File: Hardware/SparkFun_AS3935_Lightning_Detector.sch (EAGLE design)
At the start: 30 parts, among them U1 AS3935

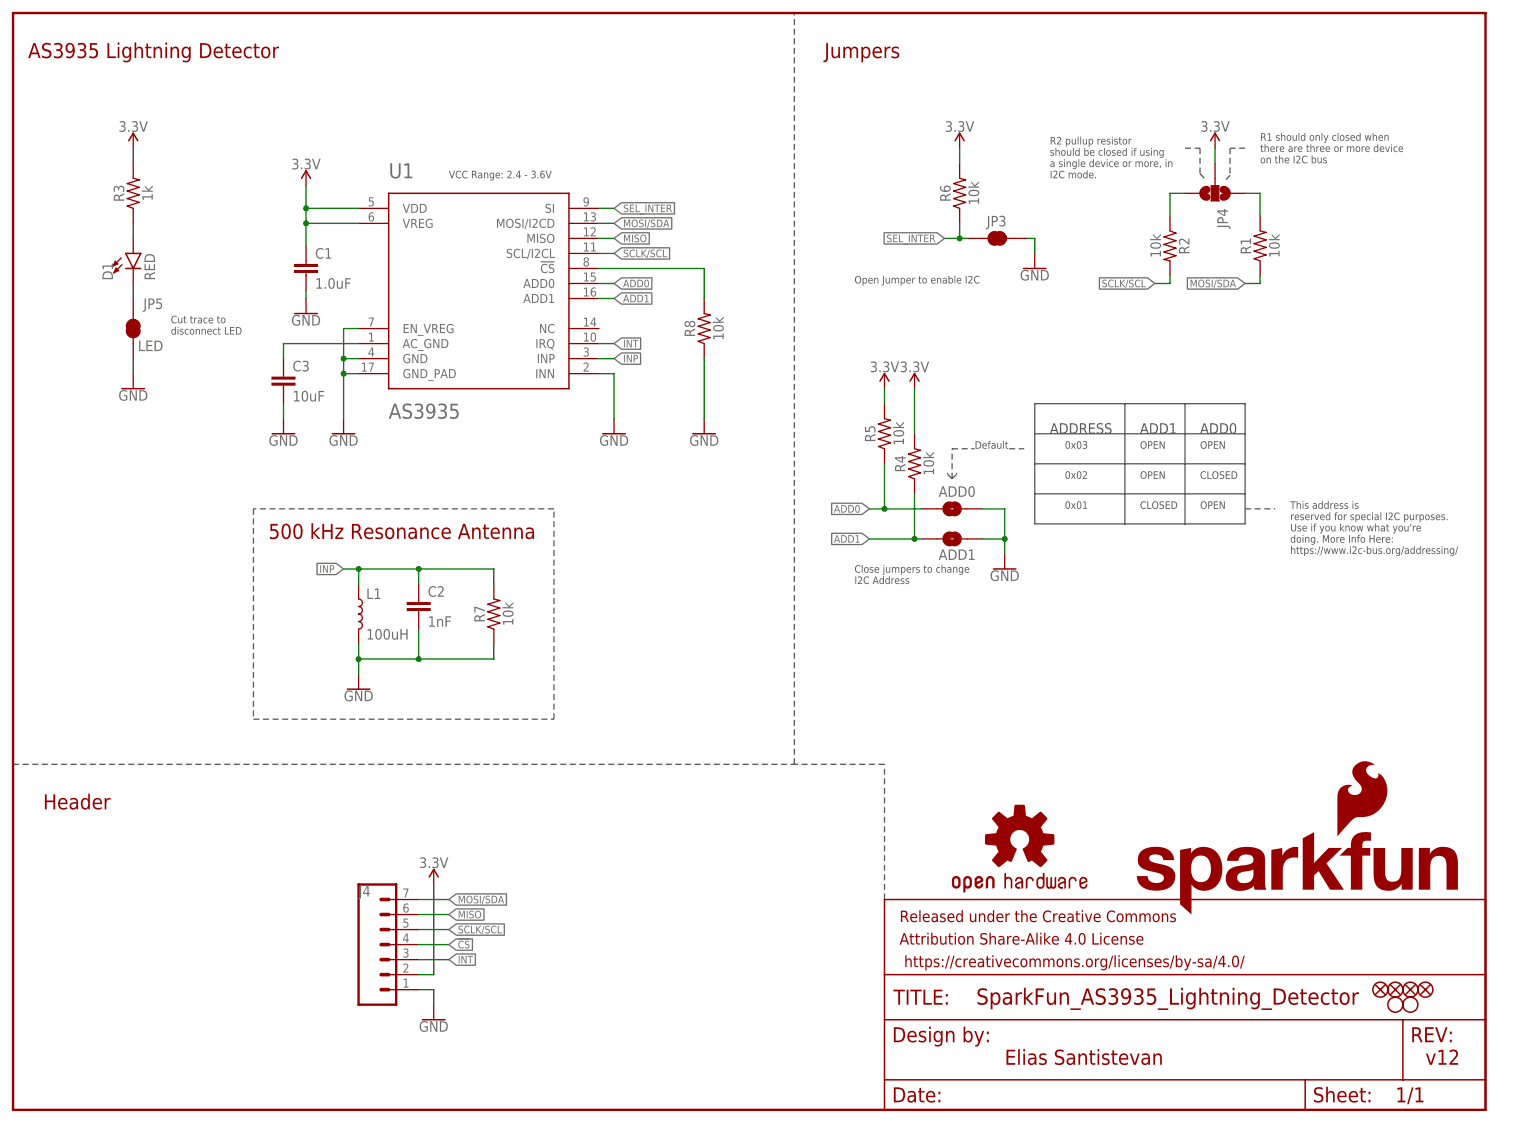
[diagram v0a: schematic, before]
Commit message: Changes chip select pull down to pullup.
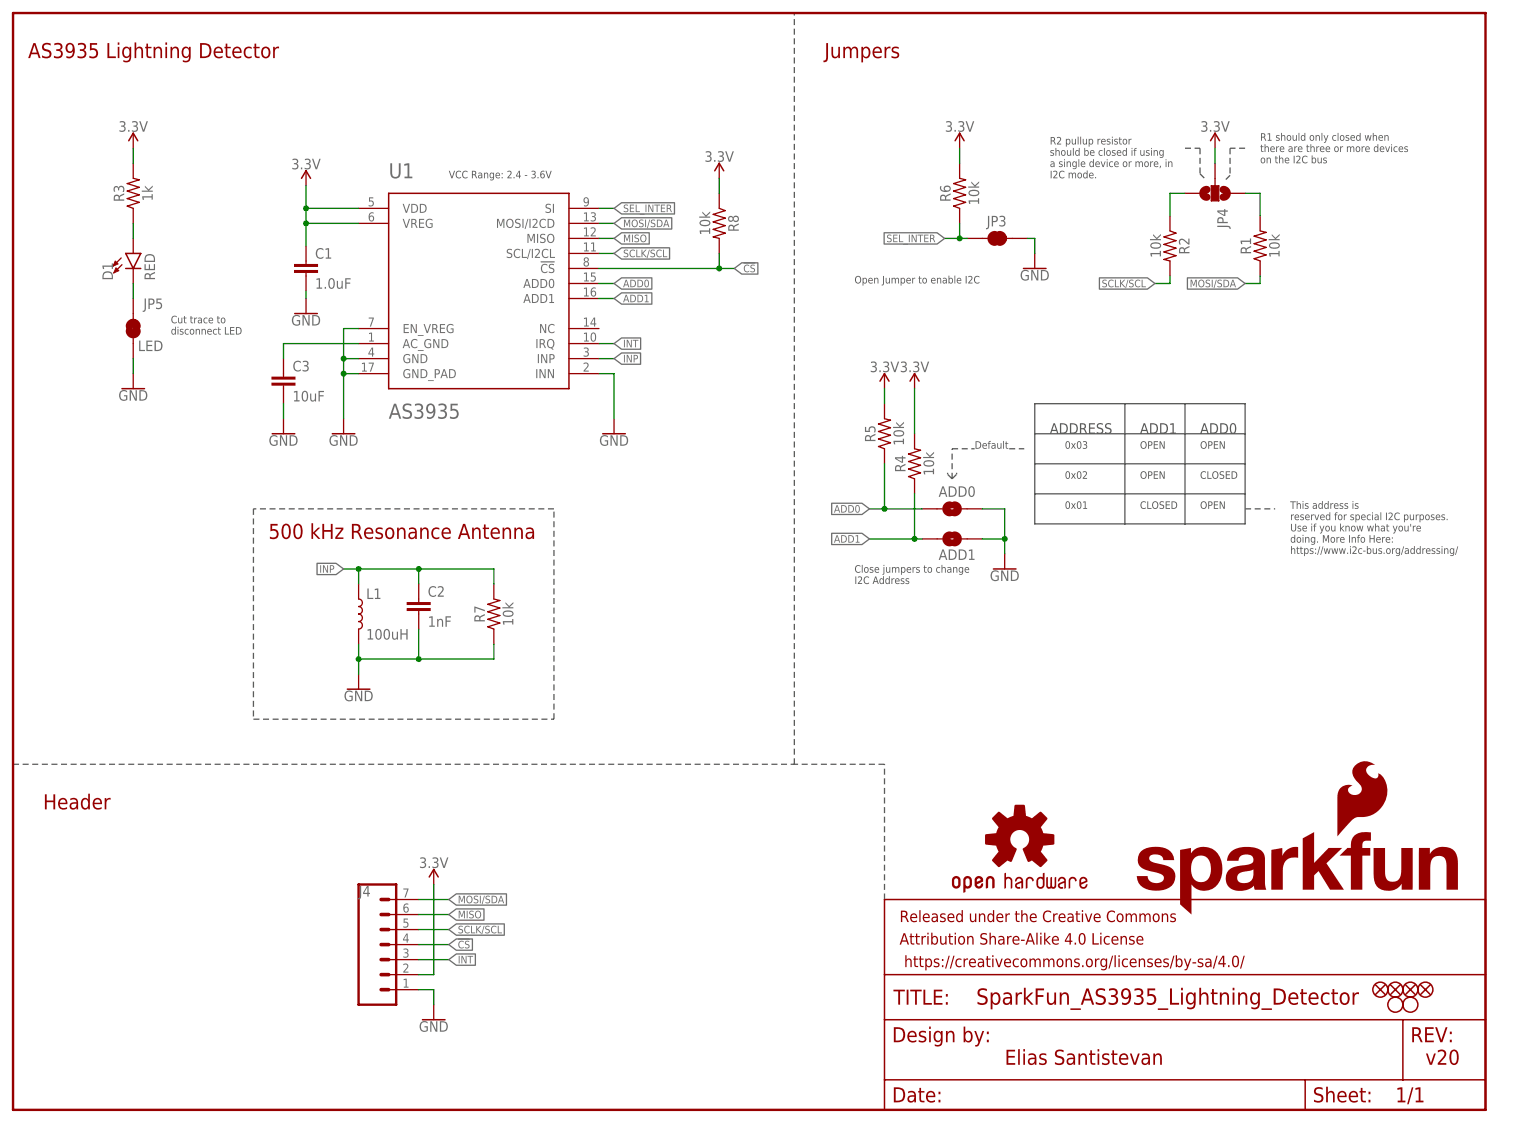
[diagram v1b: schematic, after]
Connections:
- net 3.3V: now also R8.1
- net GND: no longer R8.1
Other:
- note added: "R1 should only closed when there are three or more devices on the I2C bus"
- note added: "v20"
- note removed: "R1 should only closed when there are three or more device on the I2C bus"
- note removed: "v12"
- moved on the sheet: R8
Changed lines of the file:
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@@
 <part name="LOGO3" library="SparkFun-Aesthetics" deviceset="SFE_LOGO_FLAME" device=".2_INCH"/>
 <part name="R8" library="SparkFun-Resistors" deviceset="10KOHM" device="-0603-1/10W-1%" value="10k"/>
-<part name="GND6" library="SparkFun-PowerSymbols" deviceset="GND" device=""/>
+<part name="SUPPLY2" library="SparkFun-PowerSymbols" deviceset="3.3V" device=""/>
 </parts>
 <sheets>
@@
 <plain>
 <text x="167.64" y="7.62" size="2.54" layer="94" font="vector">Elias Santistevan</text>
-<text x="238.76" y="7.62" size="2.54" layer="94" font="vector">v12</text>
+<text x="238.76" y="7.62" size="2.54" layer="94" font="vector">v20</text>
 <wire x1="0" y1="58.42" x2="132.08" y2="58.42" width="0.2032" layer="97" style="shortdash"/>
 <wire x1="147.32" y1="35.56" x2="147.32" y2="58.42" width="0.2032" layer="97" style="shortdash"/>
@@
 <text x="142.24" y="139.7" size="1.27" layer="97" font="vector">Open Jumper to enable I2C</text>
 <text x="210.82" y="160.02" size="1.27" layer="97" font="vector">R1 should only closed when
-there are three or more device
+there are three or more devices
 on the I2C bus</text>
 <text x="142.24" y="88.9" size="1.27" layer="97" font="vector">Close jumpers to change
@@
 </instance>
 <instance part="LOGO3" gate="G$1" x="223.52" y="45.72" smashed="yes"/>
-<instance part="R8" gate="G$1" x="116.84" y="132.08" smashed="yes" rot="R90">
-<attribute name="NAME" x="115.316" y="132.08" size="1.778" layer="95" font="vector" rot="R90" align="bottom-center"/>
-<attribute name="VALUE" x="118.364" y="132.08" size="1.778" layer="96" font="vector" rot="R90" align="top-center"/>
-</instance>
-<instance part="GND6" gate="1" x="116.84" y="114.3" smashed="yes">
-<attribute name="VALUE" x="116.84" y="114.046" size="1.778" layer="96" align="top-center"/>
+<instance part="R8" gate="G$1" x="119.38" y="149.86" smashed="yes" rot="R270">
+<attribute name="NAME" x="120.904" y="149.86" size="1.778" layer="95" font="vector" rot="R270" align="bottom-center"/>
+<attribute name="VALUE" x="117.856" y="149.86" size="1.778" layer="96" font="vector" rot="R270" align="top-center"/>
+</instance>
+<instance part="SUPPLY2" gate="G$1" x="119.38" y="157.48" smashed="yes">
+<attribute name="VALUE" x="119.38" y="160.274" size="1.778" layer="96" align="bottom-center"/>
 </instance>
 </instances>
@@
 <wire x1="20.32" y1="127" x2="20.32" y2="124.46" width="0.1524" layer="91"/>
 </segment>
-<segment>
-<pinref part="R8" gate="G$1" pin="1"/>
-<pinref part="GND6" gate="1" pin="GND"/>
-<wire x1="116.84" y1="127" x2="116.84" y2="116.84" width="0.1524" layer="91"/>
-</segment>
 </net>
 <net name="3.3V" class="0">
@@
 <wire x1="203.2" y1="160.02" x2="203.2" y2="162.56" width="0.1524" layer="91"/>
 </segment>
+<segment>
+<pinref part="R8" gate="G$1" pin="1"/>
+<pinref part="SUPPLY2" gate="G$1" pin="3.3V"/>
+<wire x1="119.38" y1="154.94" x2="119.38" y2="157.48" width="0.1524" layer="91"/>
+</segment>
 </net>
 <net name="MOSI/SDA" class="0">
@@
 <segment>
 <pinref part="U1" gate="G$1" pin="!CS"/>
-<wire x1="99.06" y1="142.24" x2="116.84" y2="142.24" width="0.1524" layer="91"/>
+<wire x1="99.06" y1="142.24" x2="119.38" y2="142.24" width="0.1524" layer="91"/>
 <pinref part="R8" gate="G$1" pin="2"/>
-<wire x1="116.84" y1="142.24" x2="116.84" y2="137.16" width="0.1524" layer="91"/>
-</segment>
-</net>
+<wire x1="119.38" y1="142.24" x2="121.92" y2="142.24" width="0.1524" layer="91"/>
+<wire x1="119.38" y1="144.78" x2="119.38" y2="142.24" width="0.1524" layer="91"/>
+<junction x="119.38" y="142.24"/>
+<label x="121.92" y="142.24" size="1.27" layer="95" xref="yes"/>
+</segment>
+</net>

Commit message: Adds three way jumper for switching to I2C, one that also includes a way to ground Chip select
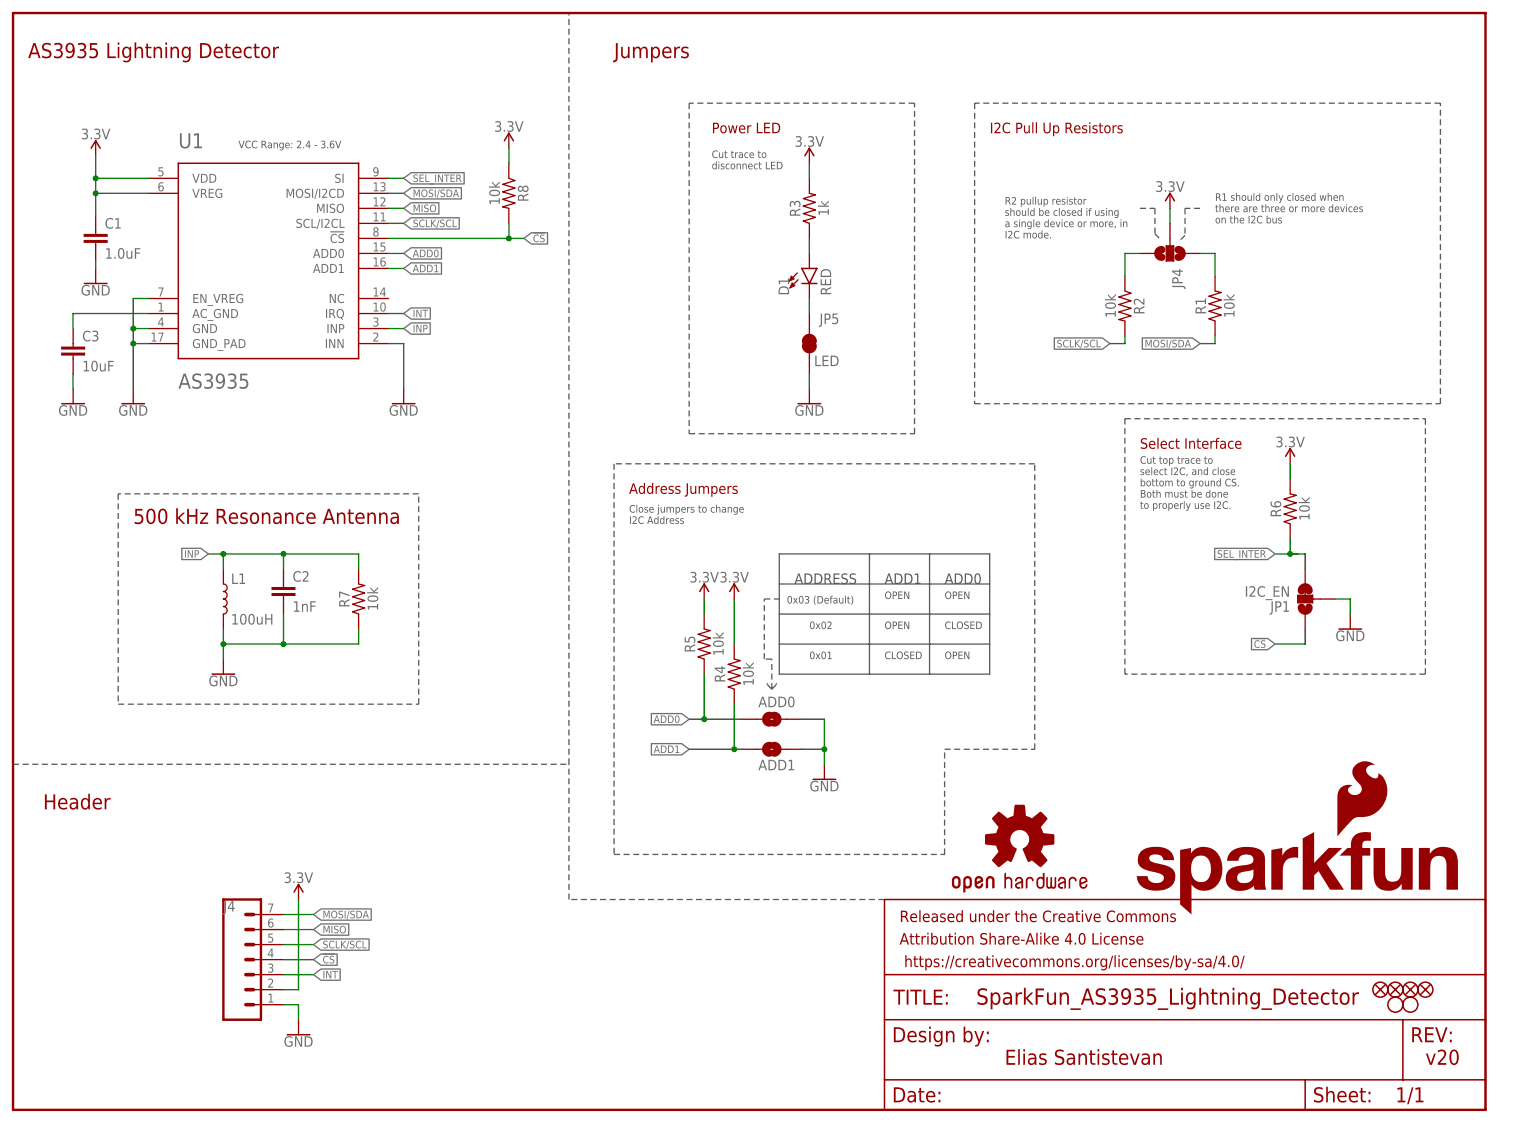
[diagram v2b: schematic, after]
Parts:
- removed JP3: JUMPER-SMT_2_NC_TRACE_SILK, SparkFun-Jumpers:JUMPER-SMT_2_NC_TRACE_SILK
- added JP1: I2C_EN, SparkFun-Jumpers:JUMPER-SMT_3_1-NC_TRACE_SILK
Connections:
- net !CS: now also JP1.1
- net GND: now also JP1.2; no longer JP3.2
- net SEL_INTER: now also JP1.3; no longer JP3.1
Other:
- note added: "0x03 (Default)"
- note added: "Address Jumpers"
- note added: "Cut top trace to select I2C, and close bottom to ground CS. Both must be done to properly use I2C."
- note added: "I2C Pull Up Resistors"
- note added: "Power LED"
- note added: "Select Interface"
- note removed: "0x03"
- note removed: "Default"
- note removed: "Open Jumper to enable I2C"
- note removed: "This address is reserved for special I2C purposes. Use if you know what you're doing. More Info Here: https://www.i2c-bus.org/addressing/"
- moved on the sheet: ADD0, ADD1, C1, C2, C3, D1, J4, JP4, JP5, L1, R1, R2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
